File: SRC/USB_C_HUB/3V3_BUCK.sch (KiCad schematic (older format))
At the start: 43 parts, among them IC4 TPS62824ADMQR, Q1 SI4842BDY-T1-GE3, Q2 SI4842BDY-T1-GE3, Q3 IRF3710ZSTRLPBF, U11 LM3478MM_NOPB, U12 LM3150MH

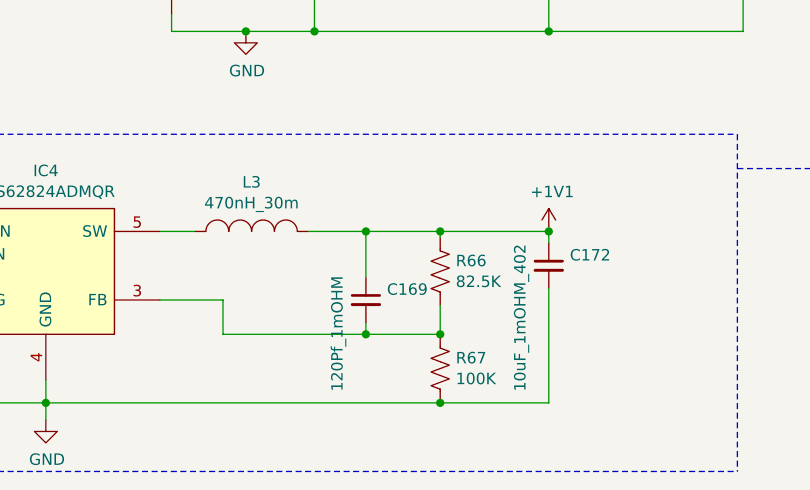
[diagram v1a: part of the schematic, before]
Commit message: schematic capture and footprint assignment complete. Pending approval
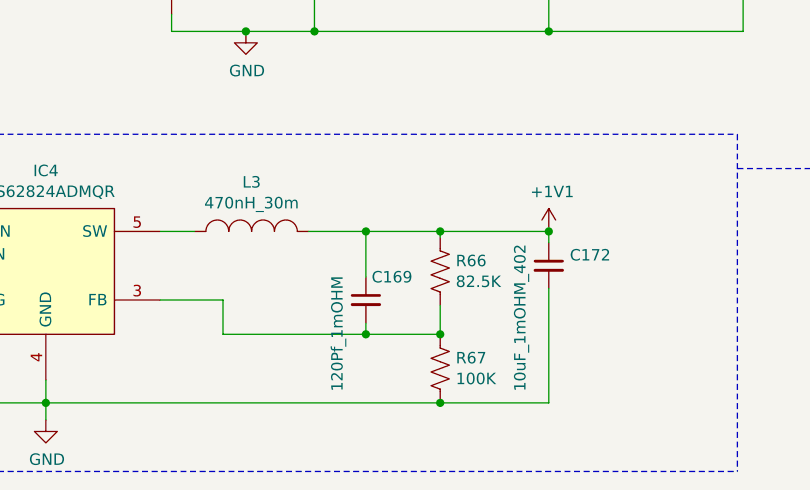
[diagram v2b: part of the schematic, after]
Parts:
- C156, C158, C159, C160, C161, C162, C163, C164, C172: footprint (none) -> Capacitor_SMD:C_0402_1005Metric
- C157: footprint (none) -> Capacitor_SMD:CP_Elec_10x10; Mfr No 6SVPE220MW -> UWT1H221MNL1GS
- C165: footprint (none) -> Capacitor_SMD:C_0402_1005Metric; Mfr No (none) -> C1005X5R1E225KT000E
- C166: footprint (none) -> Capacitor_SMD:C_0402_1005Metric; Mfr No. (none) -> GRM155R60J475ME87D
- C167: footprint (none) -> Capacitor_SMD:C_0402_1005Metric; Mfr No. (none) -> CC0402KRX7R9BB153
- C168: footprint (none) -> Capacitor_SMD:C_0402_1005Metric; Mfr No. (none) -> CC0402JRNPO9BN100
- C169: footprint (none) -> Capacitor_SMD:C_0402_1005Metric; Mfr No. (none) -> 0402CG121J500NT
- C170: footprint (none) -> Capacitor_SMD:C_0402_1005Metric; Mfr No. (none) -> CL05A474KP5NNNC
- C171, C173: footprint (none) -> Capacitor_SMD:CP_Elec_6.3x7.7
- C174: footprint (none) -> Capacitor_SMD:C_0402_1005Metric; Vendor (none) -> Digikey(DK)
- C175: footprint (none) -> Capacitor_SMD:CP_Elec_5x5.9
- D24: footprint (none) -> SamacSys_Parts_2:STPS30L30DJFTR; Mfr No. (none) -> STPS30L30DJF-TR; Vendor (none) -> DigiKey(DK)
- L2: footprint (none) -> footprints:0840CDMCCDS-1R0MC
- L3: footprint (none) -> footprints:SRP3012TA-R47M
- L4: footprint (none) -> footprints:PM4548.102NLT
- R58: footprint (none) -> Resistor_SMD:R_0603_1608Metric; Mfr No. (none) -> RMC060325.5K1%N
- R59: footprint (none) -> Resistor_SMD:R_0603_1608Metric; Mfr No. (none) -> 0603WAF2672T5E
- R60: footprint (none) -> Resistor_SMD:R_0603_1608Metric; Mfr No. (none) -> ERJPB3D1003V
- R61: footprint (none) -> Resistor_SMD:R_0603_1608Metric; mfr no. (none) -> 0603WAF1241T5E
- R62, R63, R64, R68, R69: footprint (none) -> Resistor_SMD:R_0603_1608Metric
- R65: footprint (none) -> Resistor_SMD:R_0805_2012Metric
- R66: footprint (none) -> Resistor_SMD:R_0603_1608Metric; Mfr No. (none) -> CRCW060382K5FKEA
- R67: footprint (none) -> Resistor_SMD:R_0603_1608Metric; Mfr No. (none) -> 0603WAJ0104T5E
- Ron1: footprint (none) -> Resistor_SMD:R_0805_2012Metric; Mfr No. (none) -> RMCF0805FT6K65

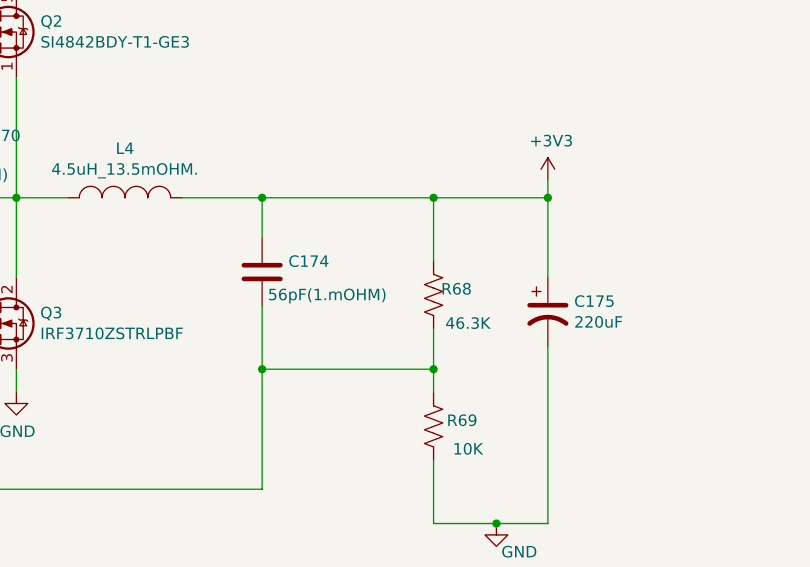
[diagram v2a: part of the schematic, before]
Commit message: updated BOM, minor change in schematic
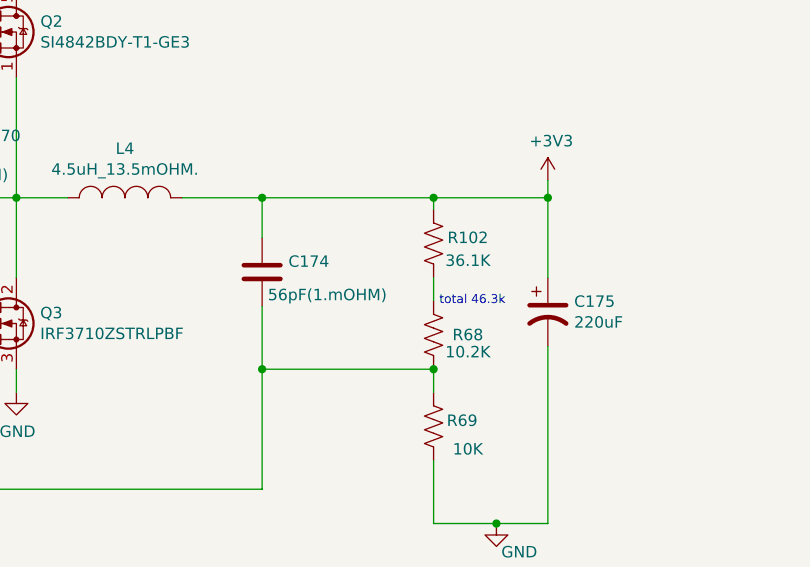
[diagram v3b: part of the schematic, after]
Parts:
- added R102: 36.1K, Resistor_SMD:R_0603_1608Metric, symbol Device:R_US
- R60: Mfr No. ERJPB3D1003V -> (none)
- R64: Mfr No. WSLP08056L000FEA18 -> (none)
- R68: value 46.3K -> 10.2K; Mfr No. (none) -> CR0603FA1022G; Vendor (none) -> Digikey
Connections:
- net +3V3: now also R102.2; no longer R68.2
- new net: R102.1, R68.2
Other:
- note added: "total 46.3k\n"
- moved on the sheet: R68
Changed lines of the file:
@@
 L Device:R_US R68
 U 1 1 61F8DE0C
-P 7625 2250
-F 0 "R68" H 7525 2225 50  0000 C CNN
-F 1 "46.3K" H 7475 2375 50  0000 C CNN
-F 2 "Resistor_SMD:R_0603_1608Metric" V 7665 2240 50  0001 C CNN
-F 3 "~" H 7625 2250 50  0001 C CNN
-	1    7625 2250
+P 7625 2425
+F 0 "R68" H 7475 2425 50  0000 C CNN
+F 1 "10.2K" H 7475 2500 50  0000 C CNN
+F 2 "Resistor_SMD:R_0603_1608Metric" V 7665 2415 50  0001 C CNN
+F 3 "~" H 7625 2425 50  0001 C CNN
+F 4 "CR0603FA1022G" H 7625 2425 50  0001 C CNN "Mfr No."
+F 5 "Digikey" H 7625 2425 50  0001 C CNN "Vendor"
+	1    7625 2425
 	-1   0    0    1
 $EndComp
-Wire Wire Line
-	7625 2100 7625 1825
-Wire Wire Line
-	7625 1825 6875 1825
 Connection ~ 6875 1825
 $Comp
@@
 	6875 2300 6875 2575
 Wire Wire Line
-	7625 2400 7625 2575
-Connection ~ 7625 2575
-Wire Wire Line
 	7625 2575 7625 2675
 Wire Wire Line
 	8125 2175 8125 1825
-Wire Wire Line
-	8125 1825 7625 1825
-Connection ~ 7625 1825
 Wire Wire Line
 	8125 2475 8125 3250
@@
 F 2 "Resistor_SMD:R_0603_1608Metric" V 5015 3965 50  0001 C CNN
 F 3 "~" H 4975 3975 50  0001 C CNN
-F 4 "WSLP08056L000FEA18" H 4975 3975 50  0001 C CNN "Mfr No."
+F 4 "" H 4975 3975 50  0001 C CNN "Mfr No."
 	1    4975 3975
 	0    -1   -1   0
@@
 F 2 "Resistor_SMD:R_0603_1608Metric" V 3190 6915 50  0001 C CNN
 F 3 "~" H 3150 6925 50  0001 C CNN
-F 4 "ERJPB3D1003V" V 3150 6925 50  0001 C CNN "Mfr No."
+F 4 "" V 3150 6925 50  0001 C CNN "Mfr No."
 	1    3150 6925
 	0    -1   -1   0
@@
 Text GLabel 875  1375 1    50   Input ~ 0
 SYS_PWR
+$Comp
+L Device:R_US R102
+U 1 1 618ADB39
+P 7625 2025
+F 0 "R102" H 7475 2000 50  0000 C CNN
+F 1 "36.1K" H 7475 2100 50  0000 C CNN
+F 2 "Resistor_SMD:R_0603_1608Metric" V 7665 2015 50  0001 C CNN
+F 3 "~" H 7625 2025 50  0001 C CNN
+F 4 "TNPW040236K1BEED" H 7625 2025 50  0001 C CNN "Mfr No."
+F 5 "DigiKey" H 7625 2025 50  0001 C CNN "Vendor"
+	1    7625 2025
+	-1   0    0    1
+$EndComp
+Wire Wire Line
+	6875 1825 7625 1825
+Connection ~ 7625 2575
+Wire Wire Line
+	7625 2275 7625 2175
+Wire Wire Line
+	7625 1875 7625 1825
+Connection ~ 7625 1825
+Wire Wire Line
+	7625 1825 8125 1825
+Text Notes 7650 2300 0    39   ~ 0
+total 46.3k\n
 $EndSCHEMATC
